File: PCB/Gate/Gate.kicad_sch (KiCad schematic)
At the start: 1004 parts, among them J1 Conn_01x03, J2 Conn_01x03

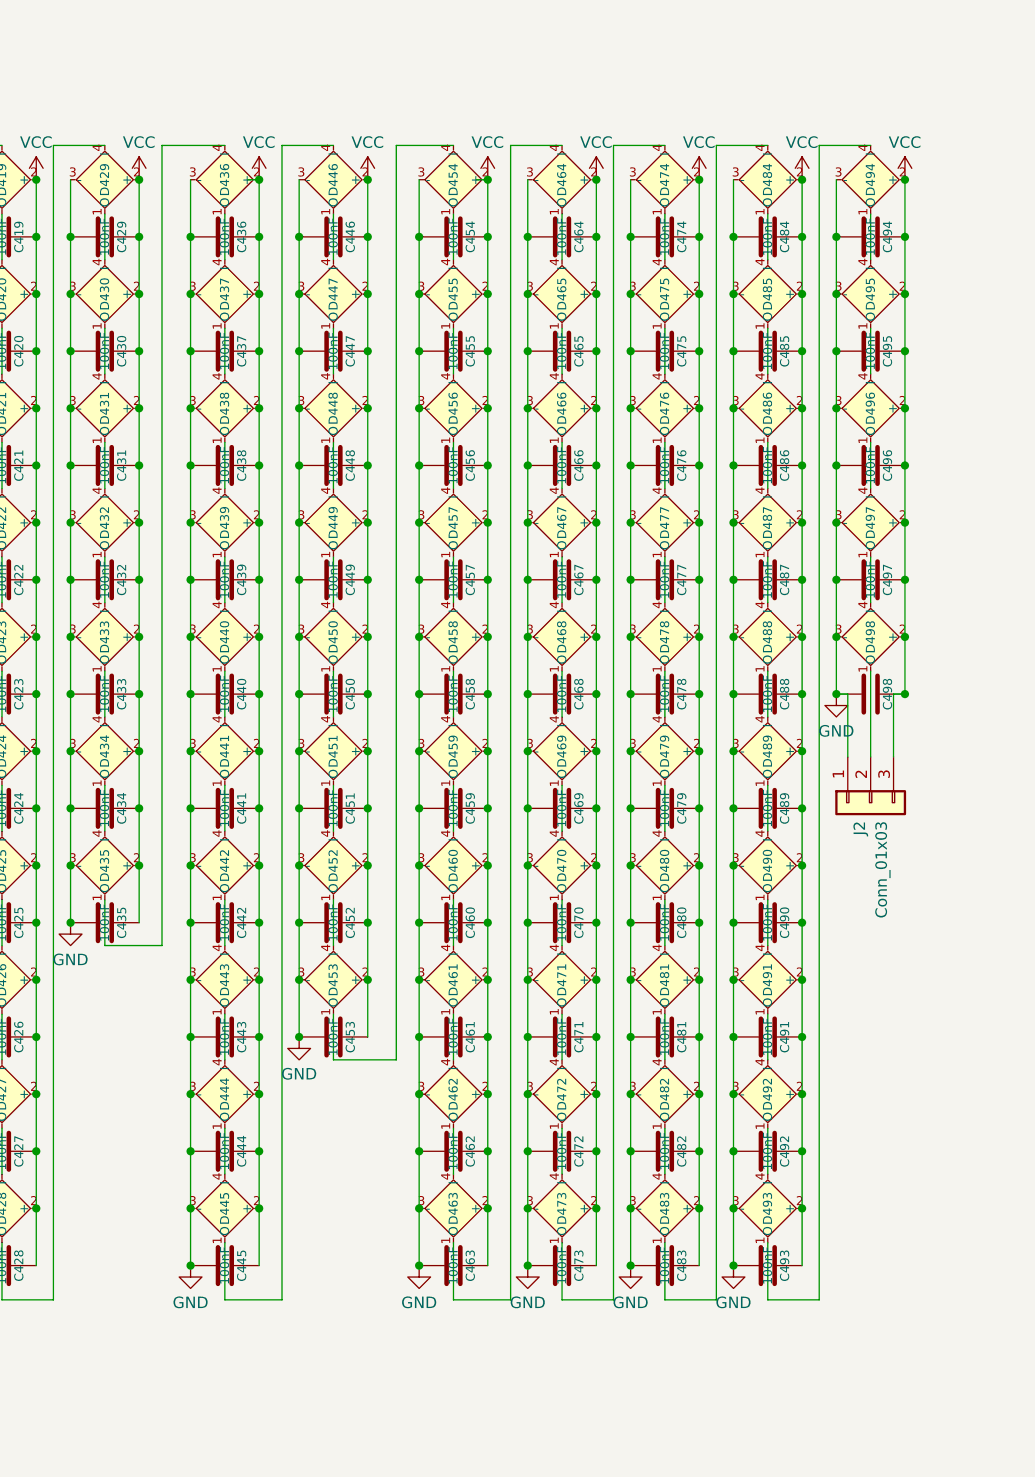
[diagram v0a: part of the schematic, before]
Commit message: 507 LEDs now
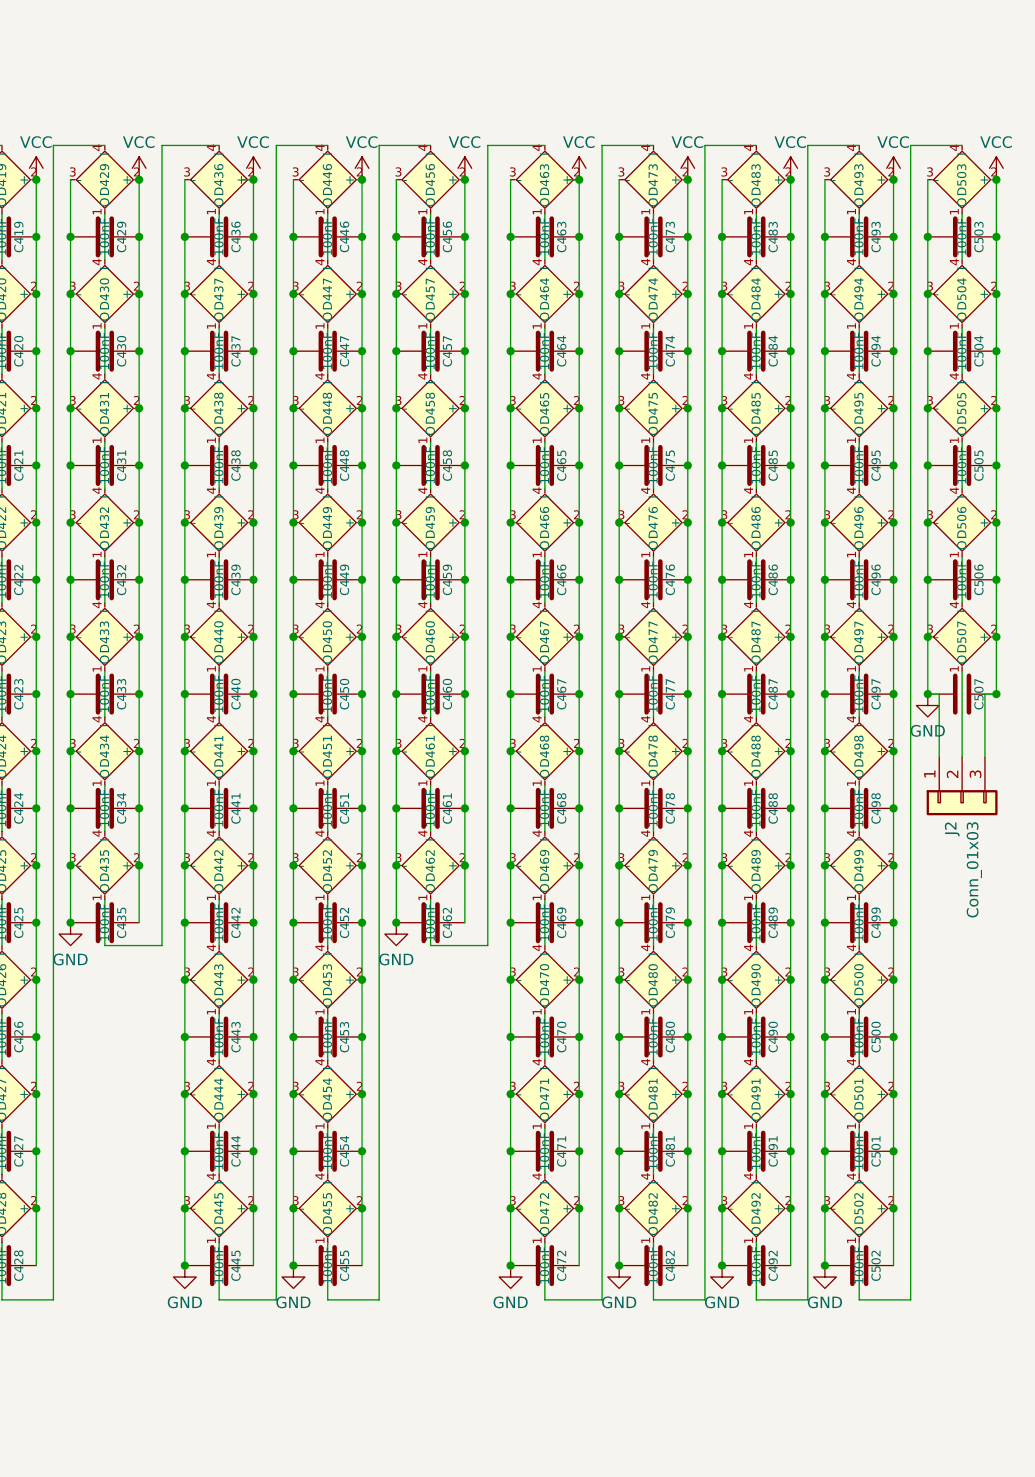
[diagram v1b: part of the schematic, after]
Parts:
- added C454, C455, C456, C457, C458, C459, C460, C461, C462: 100nF, RevK:C_0402, symbol Device:C
- added D454, D455, D456, D457, D458, D459, D460, D461, D462: XL-1010RGBC-WS2812B, RevK:SMD1010, symbol RevK:WS2812B-1mm
- renumbered C454 to C463, C455 to C464, C456 to C465, C457 to C466, C458 to C467, C459 to C468, C460 to C469, C461 to C470, C462 to C471, C463 to C472, C464 to C473, C465 to C474, C466 to C475, C467 to C476, C468 to C477, C469 to C478, C470 to C479, C471 to C480, C472 to C481, C473 to C482, C474 to C483, C475 to C484, C476 to C485, C477 to C486, C478 to C487, C479 to C488, C480 to C489, C481 to C490, C482 to C491, C483 to C492, C484 to C493, C485 to C494, C486 to C495, C487 to C496, C488 to C497, C489 to C498, C490 to C499, C491 to C500, C492 to C501, C493 to C502, C494 to C503, C495 to C504, C496 to C505, C497 to C506, C498 to C507, D454 to D463, D455 to D464, D456 to D465, D457 to D466, D458 to D467, D459 to D468, D460 to D469, D461 to D470, D462 to D471, D463 to D472, D464 to D473, D465 to D474, D466 to D475, D467 to D476, D468 to D477, D469 to D478, D470 to D479, D471 to D480, D472 to D481, D473 to D482, D474 to D483, D475 to D484, D476 to D485, D477 to D486, D478 to D487, D479 to D488, D480 to D489, D481 to D490, D482 to D491, D483 to D492, D484 to D493, D485 to D494, D486 to D495, D487 to D496, D488 to D497, D489 to D498, D490 to D499, D491 to D500, D492 to D501, D493 to D502, D494 to D503, D495 to D504, D496 to D505, D497 to D506, D498 to D507
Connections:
- net GND: now also C454.2, C455.2, C456.2, C457.2, C458.2, C459.2, C460.2, C461.2, C462.2, D454.3 (-), D455.3 (-), D456.3 (-), D457.3 (-), D458.3 (-), D459.3 (-), D460.3 (-), D461.3 (-), D462.3 (-)
- net VCC: now also C454.1, C455.1, C456.1, C457.1, C458.1, C459.1, C460.1, C461.1, C462.1, D454.2 (+), D455.2 (+), D456.2 (+), D457.2 (+), D458.2 (+), D459.2 (+), D460.2 (+), D461.2 (+), D462.2 (+)
- net at D463.4 (I): now also D462.1 (O); no longer D453.1 (O)
- new net: D460.1 (O), D461.4 (I)
- new net: D459.1 (O), D460.4 (I)
- new net: D461.1 (O), D462.4 (I)
- new net: D458.1 (O), D459.4 (I)
- new net: D457.1 (O), D458.4 (I)
- new net: D456.1 (O), D457.4 (I)
- new net: D455.1 (O), D456.4 (I)
- new net: D454.1 (O), D455.4 (I)
- new net: D453.1 (O), D454.4 (I)
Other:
- moved on the sheet: C463, C464, C465, C466, C467, C468, C469, C470, C471, C472, C473, C474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

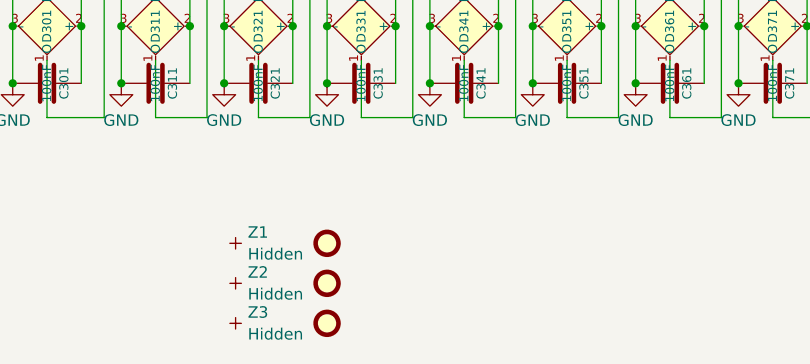
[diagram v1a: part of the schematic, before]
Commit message: Fix mounting holes
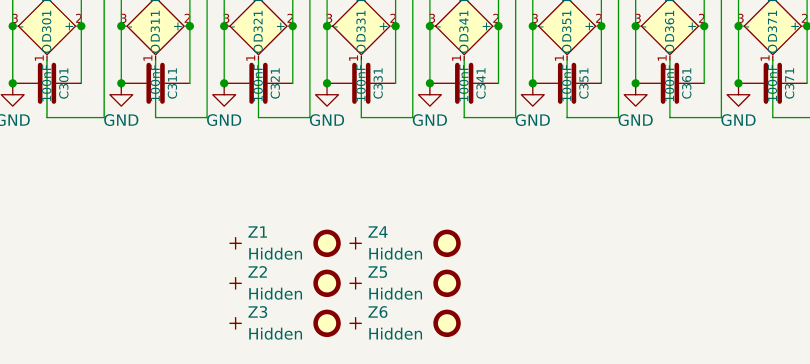
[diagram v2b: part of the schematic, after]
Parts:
- added FID4, FID5, FID6: Fiducial, RevK:Hole-Tooling, symbol Mechanical:Fiducial
- added Z4, Z5, Z6: Hidden, RevK:PCB-Join1, symbol RevK:Hidden
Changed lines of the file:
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@@
     )
   )
+  (symbol (lib_id "Mechanical:Fiducial") (at 280.035 173.99 0) (unit 1)
+    (in_bom no) (on_board yes) (dnp no) (fields_autoplaced)
+    (property "Reference" "FID5" (at 282.194 172.7779 0)
+      (effects (font (size 1.27 1.27)) (justify left) hide)
+    )
+    (property "Value" "Fiducial" (at 282.194 175.2021 0)
+      (effects (font (size 1.27 1.27)) (justify left) hide)
+    )
+    (property "Footprint" "RevK:Hole-Tooling" (at 280.035 173.99 0)
+      (effects (font (size 1.27 1.27)) hide)
+    )
+    (property "Datasheet" "~" (at 280.035 173.99 0)
+      (effects (font (size 1.27 1.27)) hide)
+    )
+    (instances
+      (project "Gate"
+        (path "/46c350bb-7de4-4e81-aafd-4af55e37aab0"
+          (reference "FID5") (unit 1)
+        )
+      )
+    )
+  )
   (symbol (lib_id "RevK:WS2812B-1mm") (at 110.49 56.515 90) (mirror x) (unit 1)
     (in_bom yes) (on_board yes) (dnp no) (fields_autoplaced)
@@
     )
   )
+  (symbol (lib_id "Mechanical:Fiducial") (at 280.035 178.435 0) (unit 1)
+    (in_bom no) (on_board yes) (dnp no) (fields_autoplaced)
+    (property "Reference" "FID6" (at 282.194 177.2229 0)
+      (effects (font (size 1.27 1.27)) (justify left) hide)
+    )
+    (property "Value" "Fiducial" (at 282.194 179.6471 0)
+      (effects (font (size 1.27 1.27)) (justify left) hide)
+    )
+    (property "Footprint" "RevK:Hole-Tooling" (at 280.035 178.435 0)
+      (effects (font (size 1.27 1.27)) hide)
+    )
+    (property "Datasheet" "~" (at 280.035 178.435 0)
+      (effects (font (size 1.27 1.27)) hide)
+    )
+    (instances
+      (project "Gate"
+        (path "/46c350bb-7de4-4e81-aafd-4af55e37aab0"
+          (reference "FID6") (unit 1)
+        )
+      )
+    )
+  )
   (symbol (lib_id "RevK:WS2812B-1mm") (at 327.66 107.315 90) (mirror x) (unit 1)
     (in_bom yes) (on_board yes) (dnp no) (fields_autoplaced)
@@
     )
   )
+  (symbol (lib_id "RevK:Hidden") (at 269.875 178.435 0) (unit 1)
+    (in_bom no) (on_board yes) (dnp no) (fields_autoplaced)
+    (property "Reference" "Z6" (at 271.2212 177.2229 0)
+      (effects (font (size 1.27 1.27)) (justify left))
+    )
+    (property "Value" "Hidden" (at 271.2212 179.6471 0)
+      (effects (font (size 1.27 1.27)) (justify left))
+    )
+    (property "Footprint" "RevK:PCB-Join1" (at 269.875 176.53 0)
+      (effects (font (size 1.27 1.27)) hide)
+    )
+    (property "Datasheet" "" (at 269.875 178.435 0)
+      (effects (font (size 1.27 1.27)) hide)
+    )
+    (property "Part No" "" (at 269.875 178.435 0)
+      (effects (font (size 1.27 1.27)) hide)
+    )
+    (property "Note" "" (at 269.875 178.435 0)
+      (effects (font (size 1.27 1.27)) hide)
+    )
+    (pin "~")
+    (instances
+      (project "Gate"
+        (path "/46c350bb-7de4-4e81-aafd-4af55e37aab0"
+          (reference "Z6") (unit 1)
+        )
+      )
+    )
+  )
   (symbol (lib_id "RevK:WS2812B-1mm") (at -42.545 132.715 90) (mirror x) (unit 1)
     (in_bom yes) (on_board yes) (dnp no) (fields_autoplaced)
@@
     )
   )
+  (symbol (lib_id "RevK:Hidden") (at 269.875 173.99 0) (unit 1)
+    (in_bom no) (on_board yes) (dnp no) (fields_autoplaced)
+    (property "Reference" "Z5" (at 271.2212 172.7779 0)
+      (effects (font (size 1.27 1.27)) (justify left))
+    )
+    (property "Value" "Hidden" (at 271.2212 175.2021 0)
+      (effects (font (size 1.27 1.27)) (justify left))
+    )
+    (property "Footprint" "RevK:PCB-Join1" (at 269.875 172.085 0)
+      (effects (font (size 1.27 1.27)) hide)
+    )
+    (property "Datasheet" "" (at 269.875 173.99 0)
+      (effects (font (size 1.27 1.27)) hide)
+    )
+    (property "Part No" "" (at 269.875 173.99 0)
+      (effects (font (size 1.27 1.27)) hide)
+    )
+    (property "Note" "" (at 269.875 173.99 0)
+      (effects (font (size 1.27 1.27)) hide)
+    )
+    (pin "~")
+    (instances
+      (project "Gate"
+        (path "/46c350bb-7de4-4e81-aafd-4af55e37aab0"
+          (reference "Z5") (unit 1)
+        )
+      )
+    )
+  )
   (symbol (lib_id "RevK:WS2812B-1mm") (at 170.815 69.215 90) (mirror x) (unit 1)
     (in_bom yes) (on_board yes) (dnp no) (fields_autoplaced)
@@
     )
   )
+  (symbol (lib_id "Mechanical:Fiducial") (at 280.035 169.545 0) (unit 1)
+    (in_bom no) (on_board yes) (dnp no) (fields_autoplaced)
+    (property "Reference" "FID4" (at 282.194 168.3329 0)
+      (effects (font (size 1.27 1.27)) (justify left) hide)
+    )
+    (property "Value" "Fiducial" (at 282.194 170.7571 0)
+      (effects (font (size 1.27 1.27)) (justify left) hide)
+    )
+    (property "Footprint" "RevK:Hole-Tooling" (at 280.035 169.545 0)
+      (effects (font (size 1.27 1.27)) hide)
+    )
+    (property "Datasheet" "~" (at 280.035 169.545 0)
+      (effects (font (size 1.27 1.27)) hide)
+    )
+    (instances
+      (project "Gate"
+        (path "/46c350bb-7de4-4e81-aafd-4af55e37aab0"
+          (reference "FID4") (unit 1)
+        )
+      )
+    )
+  )
   (symbol (lib_id "Device:C") (at 361.95 62.865 270) (mirror x) (unit 1)
     (in_bom yes) (on_board yes) (dnp no)
@@
         )
       )
+    )
+  )
+  (symbol (lib_id "RevK:Hidden") (at 269.875 169.545 0) (unit 1)
+    (in_bom no) (on_board yes) (dnp no) (fields_autoplaced)
+    (property "Reference" "Z4" (at 271.2212 168.3329 0)
+      (effects (font (size 1.27 1.27)) (justify left))
+    )
+    (property "Value" "Hidden" (at 271.2212 170.7571 0)
+      (effects (font (size 1.27 1.27)) (justify left))
+    )
+    (property "Footprint" "RevK:PCB-Join1" (at 269.875 167.64 0)
+      (effects (font (size 1.27 1.27)) hide)
+    )
+    (property "Datasheet" "" (at 269.875 169.545 0)
+      (effects (font (size 1.27 1.27)) hide)
+    )
+    (property "Part No" "" (at 269.875 169.545 0)
+      (effects (font (size 1.27 1.27)) hide)
+    )
+    (property "Note" "" (at 269.875 169.545 0)
+      (effects (font (size 1.27 1.27)) hide)
+    )
+    (pin "~")
+    (instances
+      (project "Gate"
+        (path "/46c350bb-7de4-4e81-aafd-4af55e37aab0"
+          (reference "Z4") (unit 1)
+        )
+      )

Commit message: Two holes
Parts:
- FID6: footprint RevK:Hole-Tooling -> Fiducial:Fiducial_1mm_Mask2mm
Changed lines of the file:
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@@
       (effects (font (size 1.27 1.27)) (justify left) hide)
     )
-    (property "Footprint" "RevK:Hole-Tooling" (at 280.035 178.435 0)
+    (property "Footprint" "Fiducial:Fiducial_1mm_Mask2mm" (at 280.035 178.435 0)
       (effects (font (size 1.27 1.27)) hide)
     )

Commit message: Tweek tooling holes
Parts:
- FID2, FID6: footprint Fiducial:Fiducial_1mm_Mask2mm -> RevK:Hole-Tooling
- FID4: footprint RevK:Hole-Tooling -> Fiducial:Fiducial_1mm_Mask2mm
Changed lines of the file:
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@@
       (effects (font (size 1.27 1.27)) (justify left) hide)
     )
-    (property "Footprint" "Fiducial:Fiducial_1mm_Mask2mm" (at 280.035 178.435 0)
+    (property "Footprint" "RevK:Hole-Tooling" (at 280.035 178.435 0)
       (effects (font (size 1.27 1.27)) hide)
     )
@@
       (effects (font (size 1.27 1.27)) (justify left) hide)
     )
-    (property "Footprint" "Fiducial:Fiducial_1mm_Mask2mm" (at 266.7 173.99 0)
+    (property "Footprint" "RevK:Hole-Tooling" (at 266.7 173.99 0)
       (effects (font (size 1.27 1.27)) hide)
     )
@@
       (effects (font (size 1.27 1.27)) (justify left) hide)
     )
-    (property "Footprint" "RevK:Hole-Tooling" (at 280.035 169.545 0)
+    (property "Footprint" "Fiducial:Fiducial_1mm_Mask2mm" (at 280.035 169.545 0)
       (effects (font (size 1.27 1.27)) hide)
     )

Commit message: Started on new coaster
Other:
- title: LED ring coaster -> Stargate

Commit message: PCB Update
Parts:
- D1, D10, D100, D101, D102, D103, D104, D105, D106, D107, D108, D109, D11, D110, D111, D112, D113, D114, D115, D116, D117, D118, D119, D12, D120, D121, D122, D123, D124, D125, D126, D127, D128, D129, D13, D130, D131, D132, D133, D134, D135, D136, D137, D138, D139, D14, D140, D141, D142, D143, D144, D145, D146, D147, D148, D149, D15, D150, D151, D152, D153, D154, D155, D156, D157, D158, D159, D16, D160, D161, D162, D163, D164, D165, D166, D167, D168, D169, D17, D170, D171, D172, D173, D174, D175, D176, D177, D178, D179, D18, D180, D181, D182, D183, D184, D185, D186, D187, D188, D189, D19, D190, D191, D192, D193, D194, D195, D196, D197, D198, D199, D2, D20, D200, D201, D202, D203, D204, D205, D206, D207, D208, D209, D21, D210, D211, D212, D213, D214, D215, D216, D217, D218, D219, D22, D220, D221, D222, D223, D224, D225, D226, D227, D228, D229, D23, D230, D231, D232, D233, D234, D235, D236, D237, D238, D239, D24, D240, D241, D242, D243, D244, D245, D246, D247, D248, D249, D25, D250, D251, D252, D253, D254, D255, D256, D257, D258, D259, D26, D260, D261, D262, D263, D264, D265, D266, D267, D268, D269, D27, D270, D271, D272, D273, D274, D275, D276, D277, D278, D279, D28, D280, D281, D282, D283, D284, D285, D286, D287, D288, D289, D29, D290, D291, D292, D293, D294, D295, D296, D297, D298, D299, D3, D30, D300, D301, D302, D303, D304, D305, D306, D307, D308, D309, D31, D310, D311, D312, D313, D314, D315, D316, D317, D318, D319, D32, D320, D321, D322, D323, D324, D325, D326, D327, D328, D329, D33, D330, D331, D332, D333, D334, D335, D336, D337, D338, D339, D34, D340, D341, D342, D343, D344, D345, D346, D347, D348, D349, D35, D350, D351, D352, D353, D354, D355, D356, D357, D358, D359, D36, D360, D361, D362, D363, D364, D365, D366, D367, D368, D369, D37, D370, D371, D372, D373, D374, D375, D376, D377, D378, D379, D38, D380, D381, D382, D383, D384, D385, D386, D387, D388, D389, D39, D390, D391, D392, D393, D394, D395, D396, D397, D398, D399, D4, D40, D400, D401, D402, D403, D404, D405, D406, D407, D408, D409, D41, D410, D411, D412, D413, D414, D415, D416, D417, D418, D419, D42, D420, D421, D422, D423, D424, D425, D426, D427, D428, D429, D43, D430, D431, D432, D433, D434, D435, D436, D437, D438, D439, D44, D440, D441, D442, D443, D444, D445, D446, D447, D448, D449, D45, D450, D451, D452, D453, D454, D455, D456, D457, D458, D459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: LCSC Part # C5349953 -> (none); MPN (none) -> C5349953
